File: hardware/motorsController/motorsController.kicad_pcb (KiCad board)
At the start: 2 copper layers, 176.9 x 59.3 mm, 76 parts, among them J1 batery_connector, J10 batery_connector, J11 Conn_01x04, J2 Screw_Terminal_01x01, J3 Screw_Terminal_01x01, J4 Screw_Terminal_01x01, J5 Screw_Terminal_01x01, J6 Screw_Terminal_01x01, J7 Screw_Terminal_01x01, J8 Screw_Terminal_01x01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

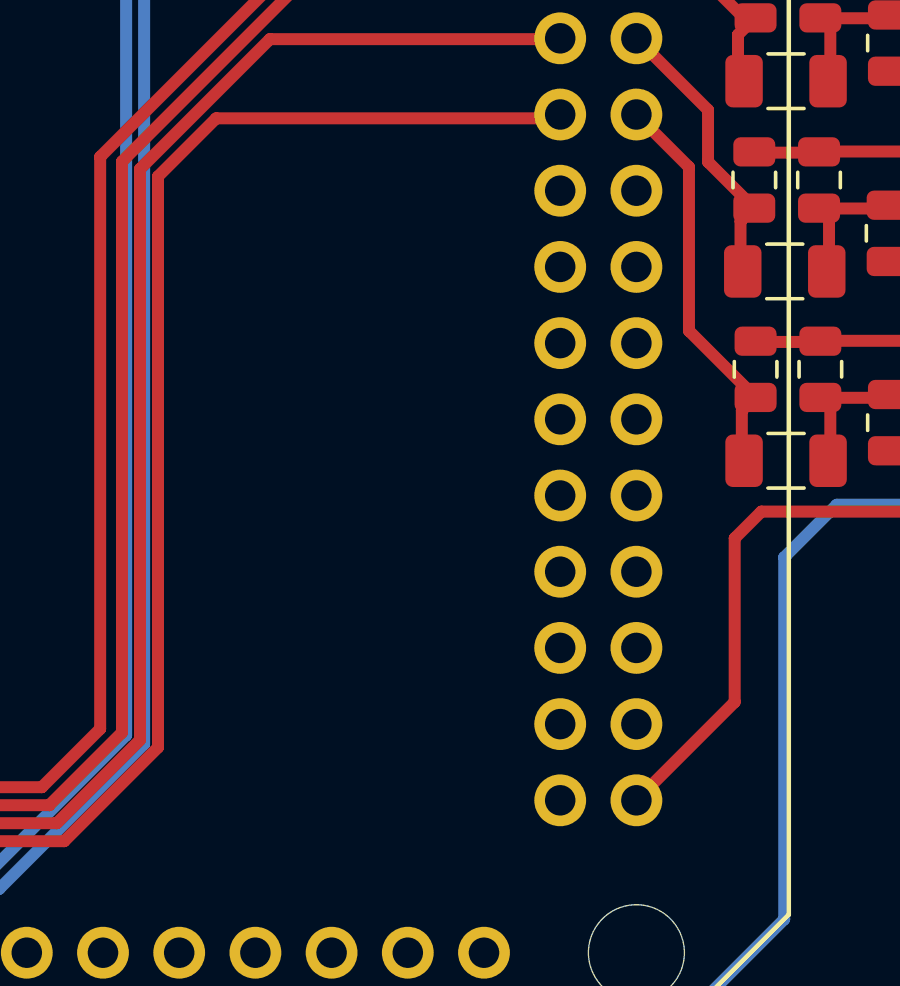
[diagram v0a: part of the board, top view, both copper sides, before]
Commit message: layout indicator leds on a pcb
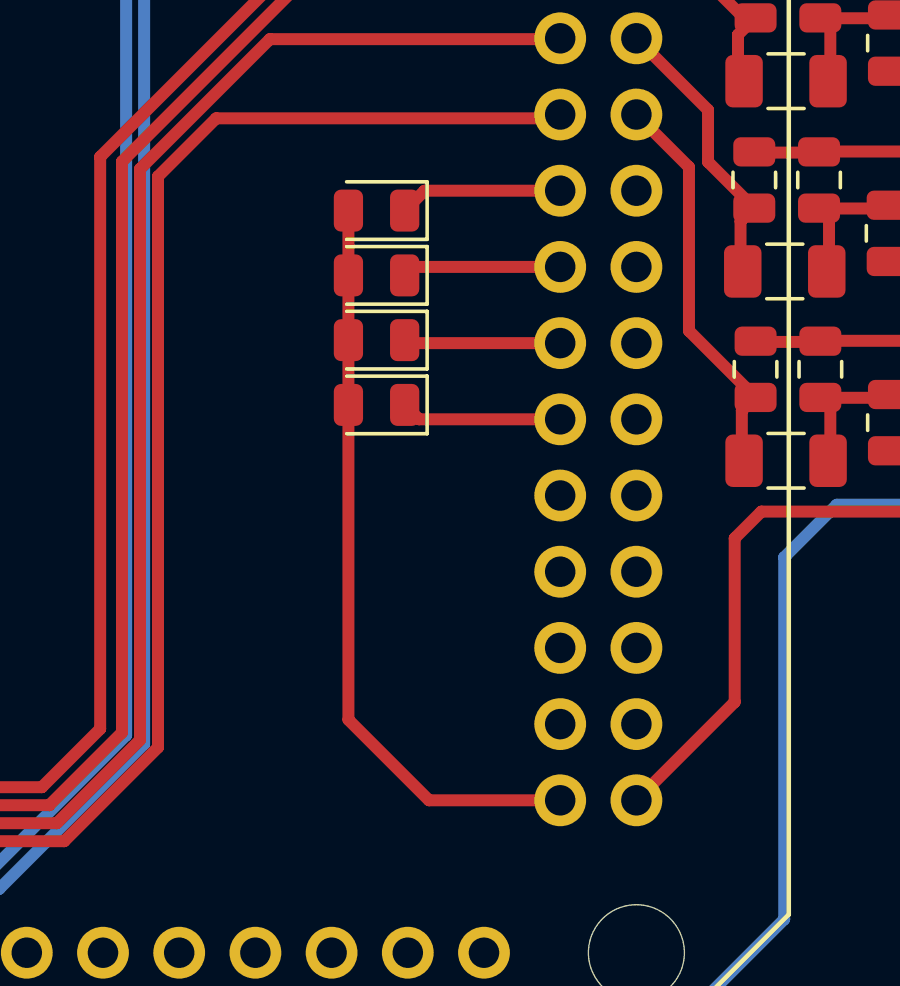
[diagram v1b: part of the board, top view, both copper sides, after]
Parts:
- added D5: LED, LED_SMD:LED_0805_2012Metric, F.Cu at (185.2, 56.9)
- added D6: LED, LED_SMD:LED_0805_2012Metric, F.Cu at (185.2, 54.7)
- added D7: LED, LED_SMD:LED_0805_2012Metric, F.Cu at (185.2, 52.6)
- added D8: LED, LED_SMD:LED_0805_2012Metric, F.Cu at (185.2, 50.4)
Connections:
- XA1 pad D38: Net-(XA1-PadD38) -> /led_1
- XA1 pad D40: Net-(XA1-PadD40) -> /led_2
- XA1 pad D42: Net-(XA1-PadD42) -> /led_3
- XA1 pad D44: Net-(XA1-PadD44) -> /led_4
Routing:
- net GND: track 756.4 -> 781.6 mm
- net /led_1: track 0.00 -> 5.46 mm
- net /led_4: track 0.00 -> 5.38 mm
- net /led_2: track 0.00 -> 5.30 mm
- net /led_3: track 0.00 -> 5.22 mm

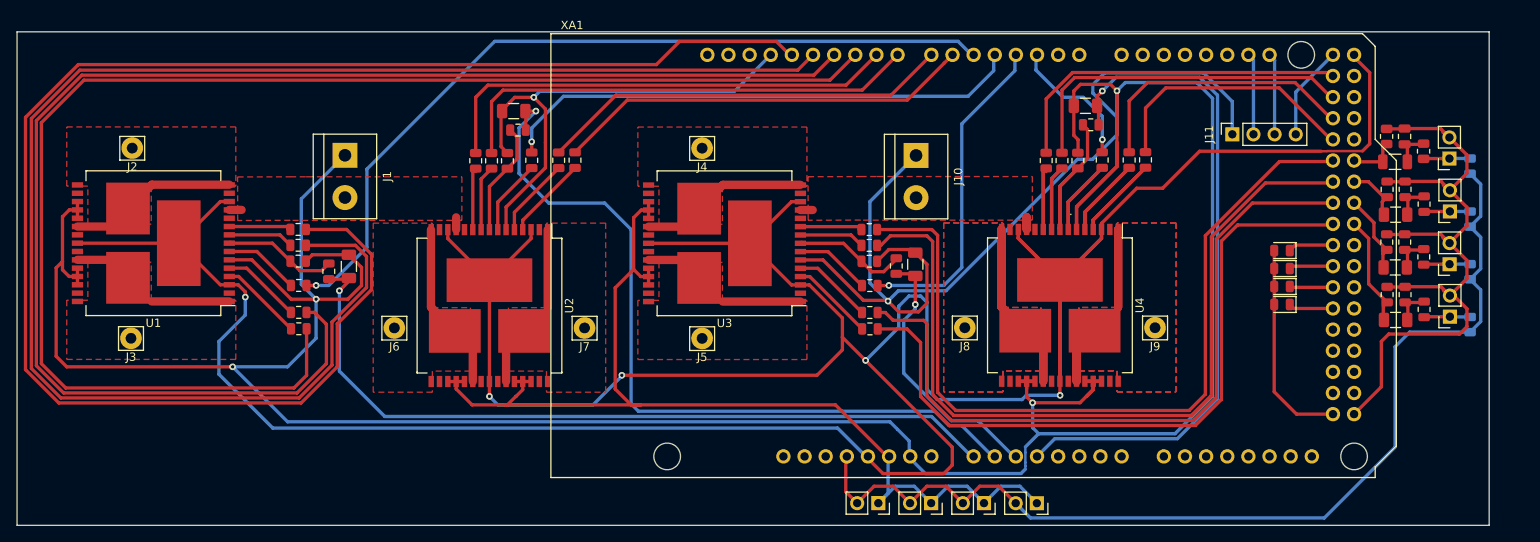
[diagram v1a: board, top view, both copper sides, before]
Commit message: increase tracks clearance
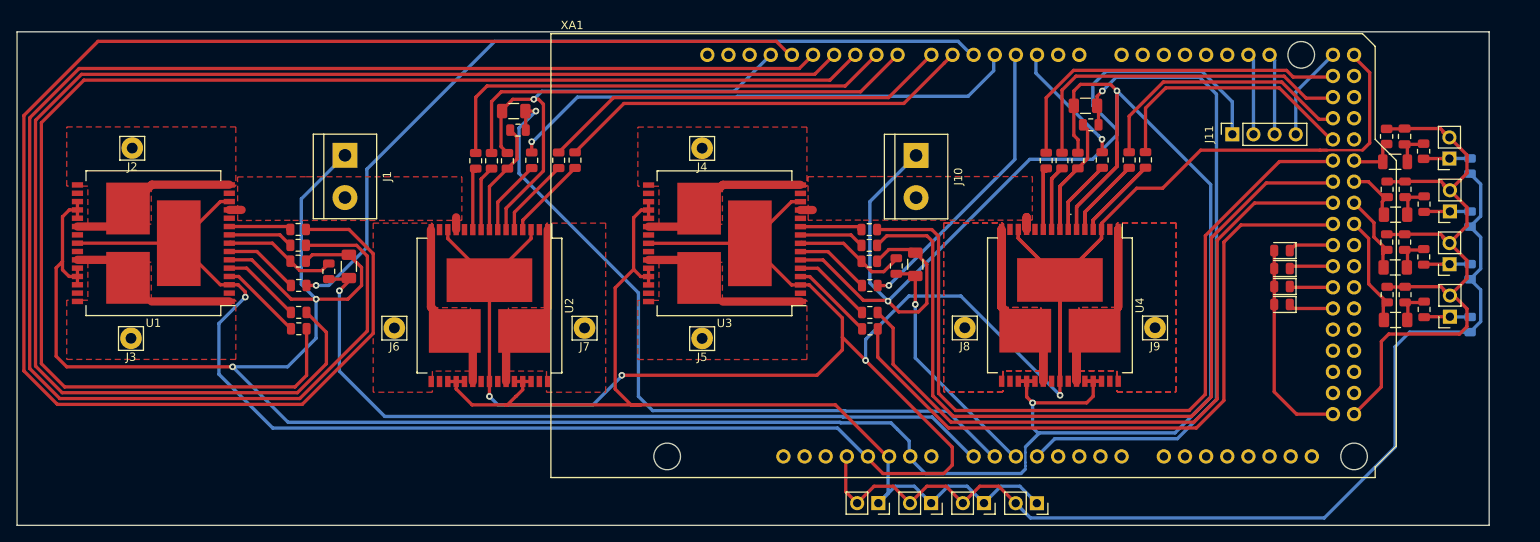
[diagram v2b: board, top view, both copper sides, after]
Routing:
- net GND: track 781.6 -> 772.7 mm
- net +5V: track 429.1 -> 422.6 mm
- net /motor_left_front_cs: track 95.9 -> 90.3 mm
- net /motor_right_rear_pwm: track 39.1 -> 35.2 mm
- net /motor_right_rear_cs: track 32.2 -> 29.2 mm
- net /motor_right_rear_diag_a: track 87.1 -> 84.7 mm
- net /motor_right_rear_fwd: track 84.3 -> 82.8 mm
- net /motor_left_rear_pwm: track 16.3 -> 14.9 mm
- net /motor_right_front_back: track 192.1 -> 193.3 mm
- net /motor_left_front_pwm: track 63.2 -> 62.2 mm
- net /motor_left_rear_diag_a: track 33.6 -> 32.6 mm
- net /motor_right_front_diag_b: track 188.8 -> 189.6 mm
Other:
- net class Default: clearance 0.2 -> 0.3; trace_width 0.25 -> 0.4
- rule trace_clearance: 0.2 -> 0.3

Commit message: increase vias' diameter for one driver
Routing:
- net GND: track 772.7 -> 776.8 mm
- net /motor_right_front_pwm: track 98.4 -> 100.3 mm
- net +5V: track 422.6 -> 424.0 mm
- net /motor_right_front_cs: track 94.5 -> 93.6 mm

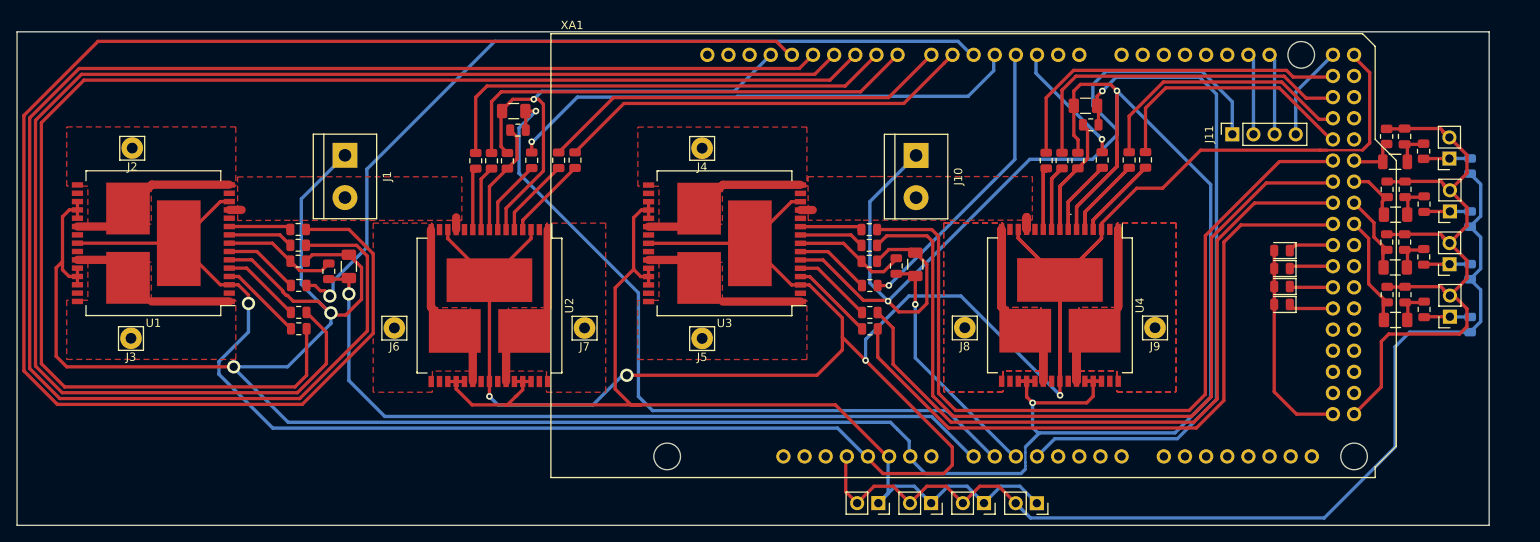
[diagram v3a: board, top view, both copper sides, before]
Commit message: move encoders' power connectors close to signals
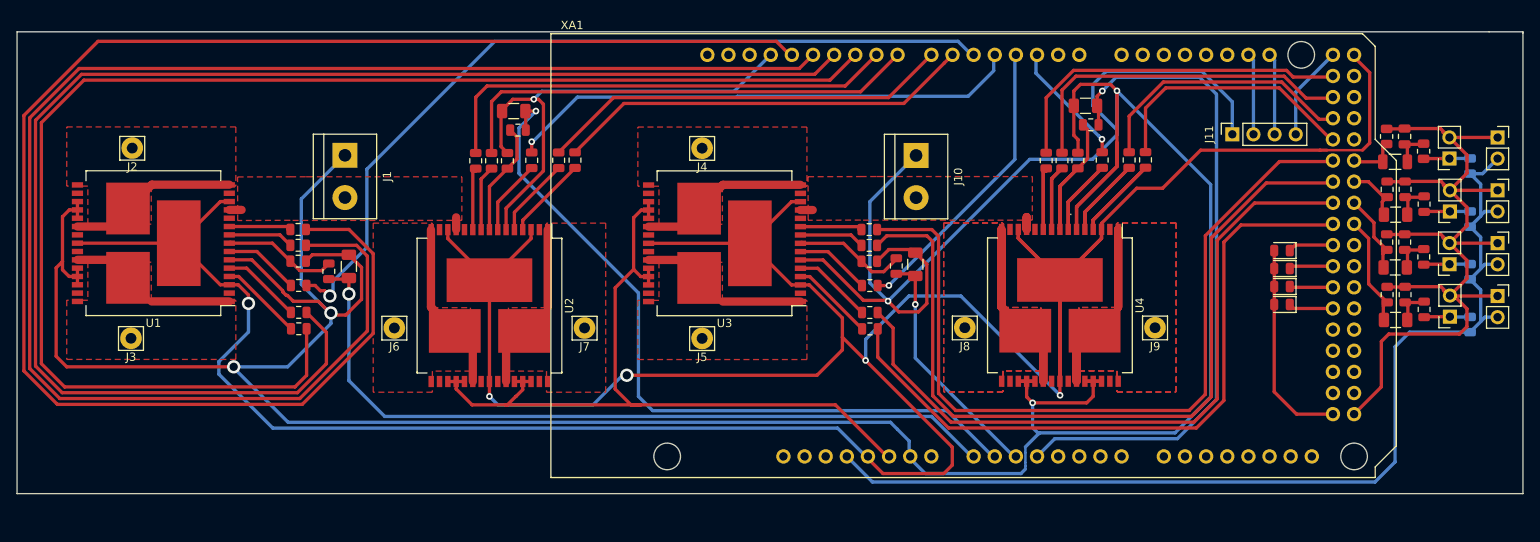
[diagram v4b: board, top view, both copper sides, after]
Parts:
- moved D1 86.4 mm to (211.1, 36.8), turned to 0 degrees
- moved D2 77.8 mm to (211.1, 43.2), turned to 0 degrees
- moved D4 69.2 mm to (211.1, 49.5), turned to 0 degrees
- moved D3 60.7 mm to (211.1, 55.9), turned to 0 degrees
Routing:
- net GND: track 776.8 -> 770.3 mm
- net +3V3: track 124.0 -> 125.3 mm
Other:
- board size 176.9 x 59.3 mm -> 181 x 55.5 mm

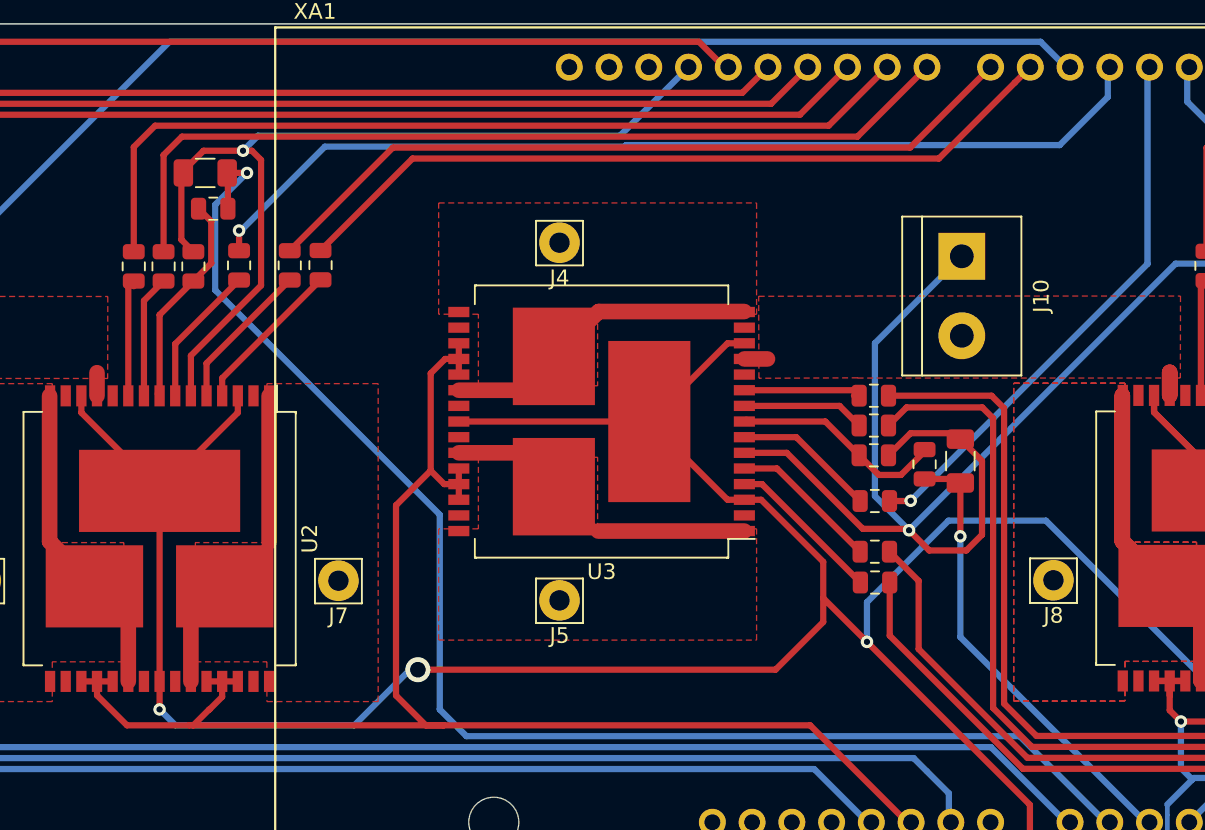
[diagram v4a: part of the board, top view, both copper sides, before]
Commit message: increase vias' dieamter for front-left driver
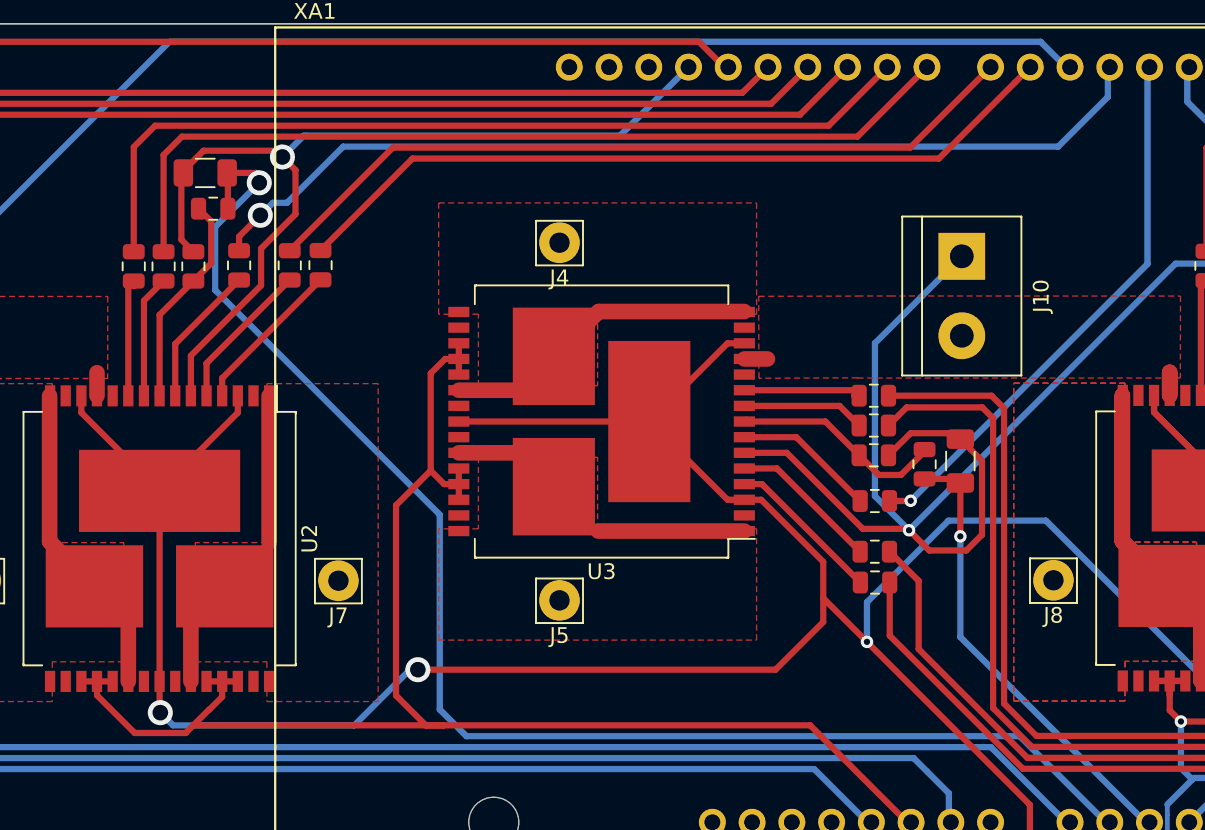
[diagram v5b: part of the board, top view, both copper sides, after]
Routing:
- net GND: track 770.3 -> 771.4 mm
- net /motor_left_front_cs: track 90.3 -> 91.3 mm

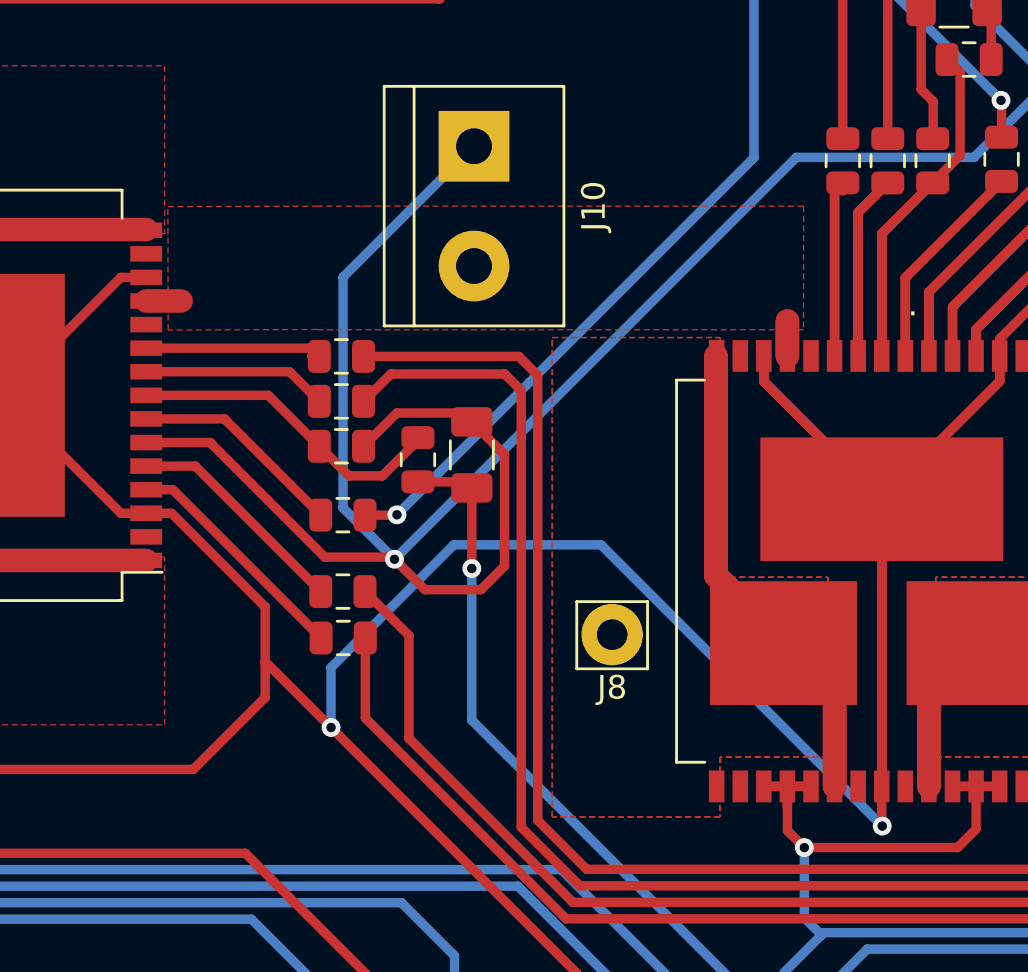
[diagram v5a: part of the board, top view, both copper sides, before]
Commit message: increase vias' dieamter for rear-right driver
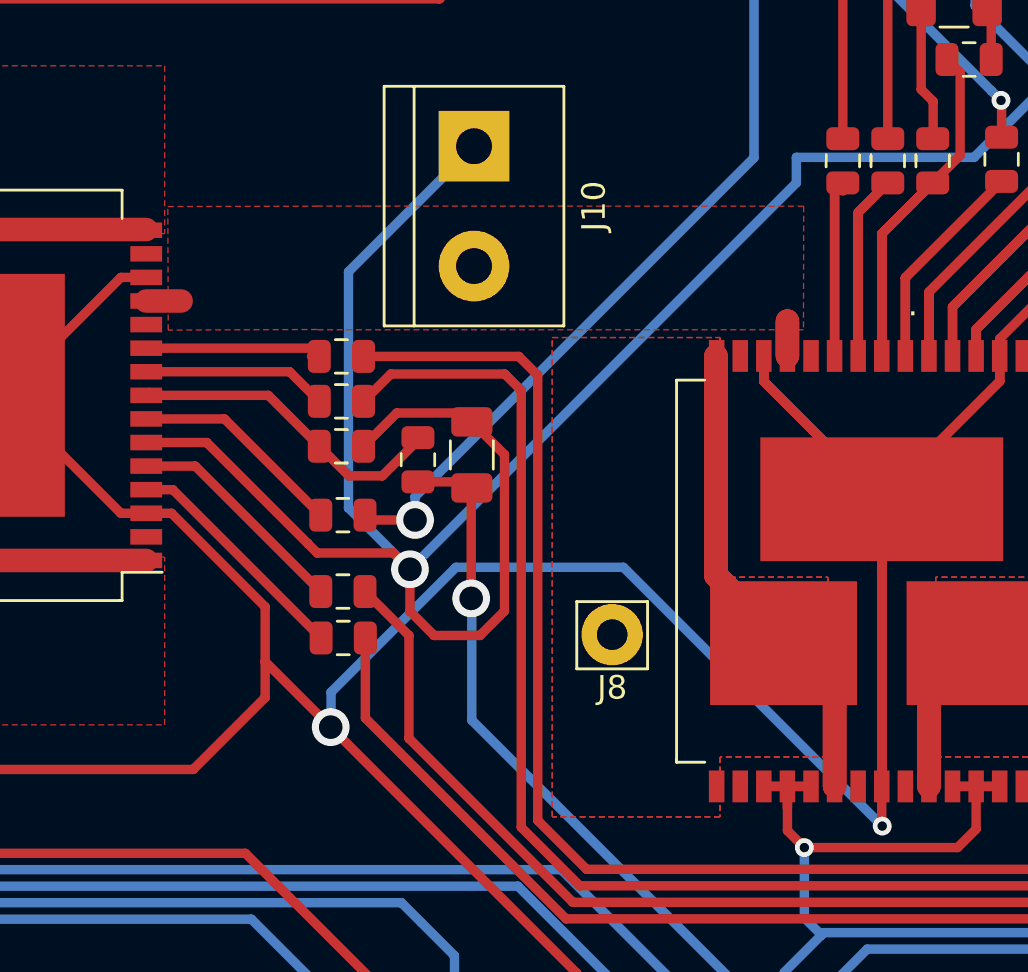
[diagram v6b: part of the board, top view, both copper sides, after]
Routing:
- net GND: track 771.4 -> 775.8 mm
- net +5V: track 424.1 -> 422.7 mm
- net /motor_right_rear_pwm: track 35.2 -> 36.2 mm
